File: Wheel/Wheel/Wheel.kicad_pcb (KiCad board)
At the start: 2 copper layers, 162 x 112 mm, 129 parts, among them J1 Conn_02x09_Odd_Even, J10 RJ45, J11 Screw_Terminal_01x02, J12 DS-201, J13 Conn_01x04, J14 Conn_02x13_Top_Bottom, J15 DB25_Female, J16 Conn_01x06, J17 Conn_01x07, J18 Conn_01x06, J19 RJ45, J2 RJ45, J20 DB9_Male, J21 DB9_Female, J22 Conn_02x15_Odd_Even, J3 RJ45, J4 RJ45, J5 USB_B, J6 Conn_02x10_Odd_Even, J7 Conn_02x09_Odd_Even, J8 RJ45, J9 RJ45, U1 MCP23S17_SP, U10 PC817, U11 IP4220CZ6, U12 PC817, U13 IP4220CZ6, U2 STM32F407VETx, U3 MCP23S17_SP, U4 USBLC6-2SC6, U5 AMS1117, U6 4N35, U7 PC817, U8 PC817, U9 PC817, Y1 32,768 кГц, Y2 8MHz

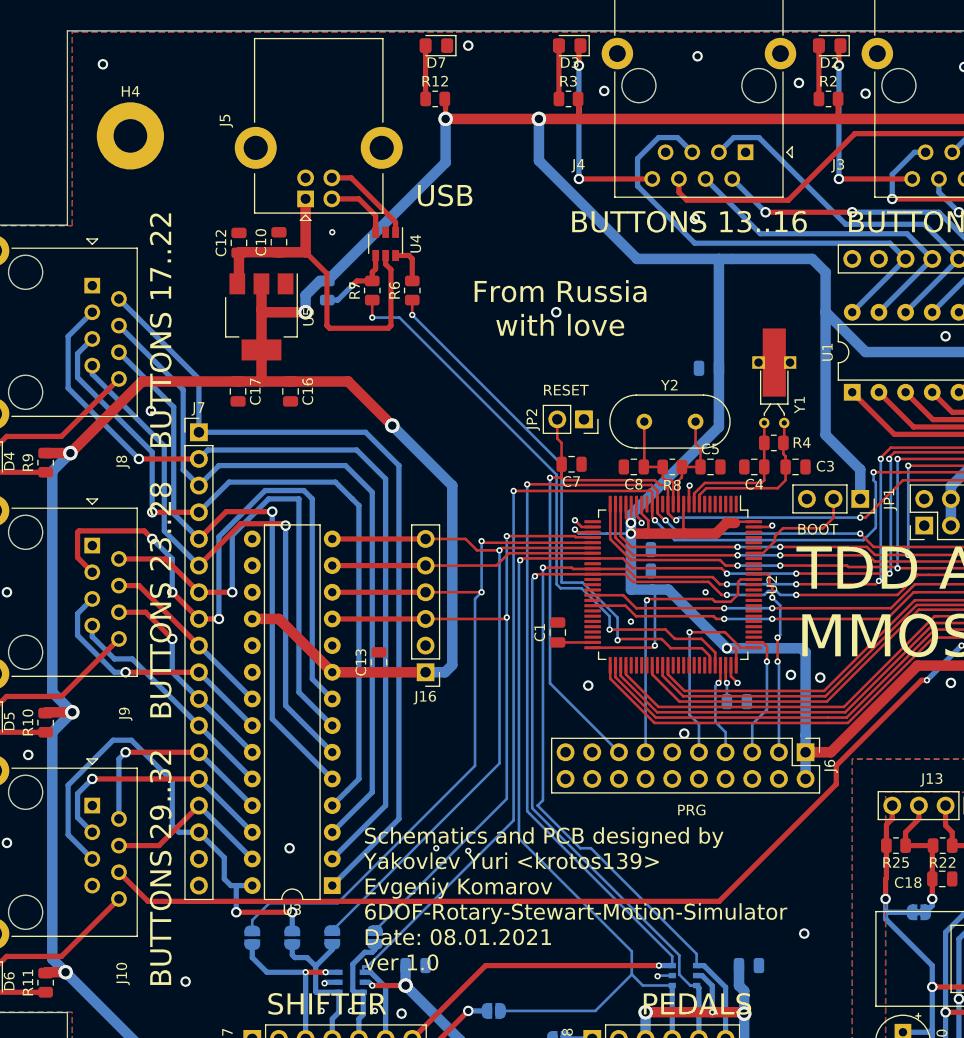
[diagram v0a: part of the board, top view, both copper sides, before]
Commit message: I've modified Wheel's scheme and PCB
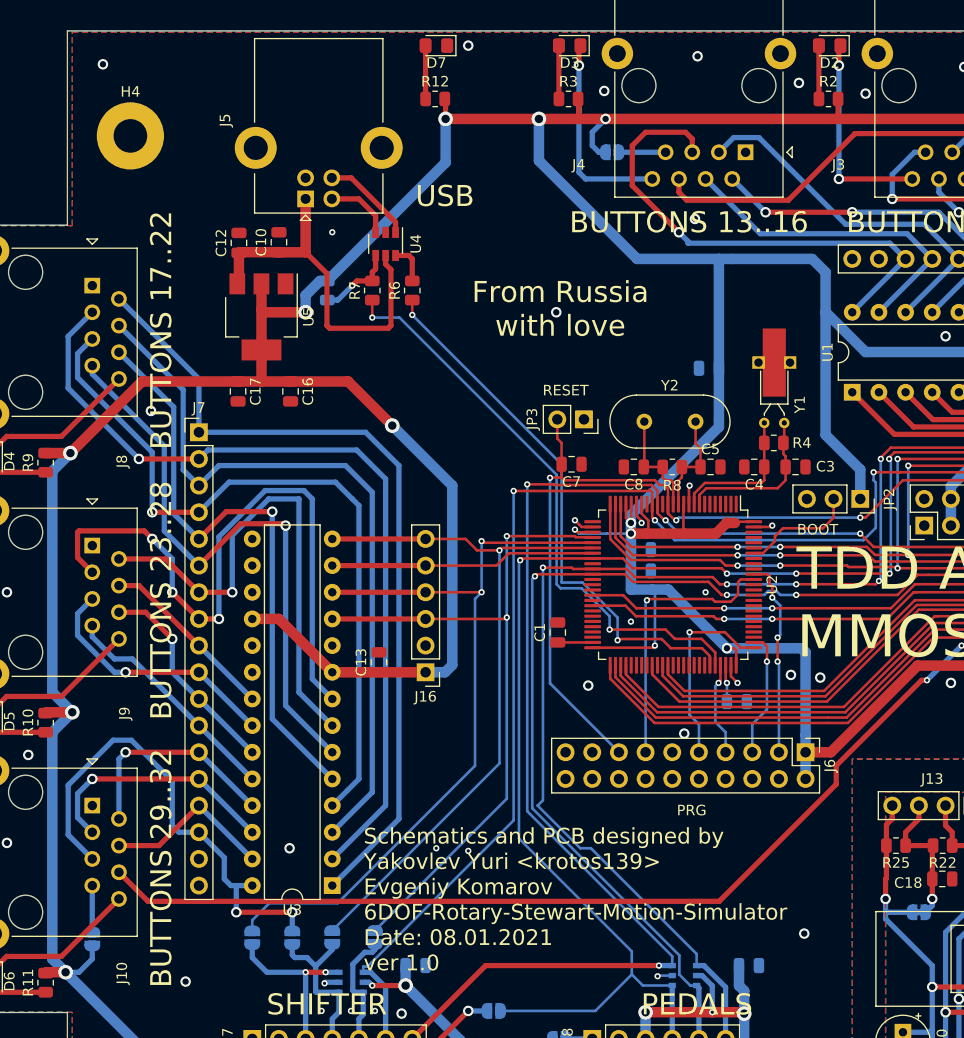
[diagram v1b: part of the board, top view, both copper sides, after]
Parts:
- added JP1: SolderJumper_2_Open, Jumper:SolderJumper-2_P1.3mm_Open_RoundedPad1.0x1.5mm, B.Cu at (91.4, 35.6)
- added JP4: SolderJumper_2_Open, Jumper:SolderJumper-2_P1.3mm_Open_RoundedPad1.0x1.5mm, B.Cu at (41.9, 110.5)
- renumbered JP8 to JP10, JP9 to JP11, JP10 to JP12, JP11 to JP13, JP12 to JP14, JP13 to JP15, JP1 to JP2, JP2 to JP3, JP3 to JP5, JP4 to JP6, JP5 to JP7, JP6 to JP8, JP7 to JP9
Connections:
- J10 pad 7: GND -> Net-(J10-Pad7)
- J4 pad 7: GND -> Net-(J4-Pad7)
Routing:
- net 3V: track 764.0 -> 772.9 mm, vias 18 -> 19
- net Net-(J10-Pad7): track 0.00 -> 4.45 mm
- net Net-(J4-Pad7): track 0.00 -> 4.44 mm
- net /B16: track 44.8 -> 47.8 mm, vias 0 -> 1
- net Net-(D3-Pad1): track 19.7 -> 19.4 mm, vias 2 -> 1
